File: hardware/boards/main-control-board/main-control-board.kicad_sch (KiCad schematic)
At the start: 7 parts, among them J2 Conn_OLED, J3 Conn_extension, J4 Conn_extension_2

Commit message: pre-fab improvements
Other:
- sheet ESP32 ports: added USB_DP; removed UDB_DP
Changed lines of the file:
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@@
 	(title_block
 		(title "TinyEngineer PCB")
-		(date "2026-09-12")
-		(rev "v1")
+		(date "2026-09-24")
+		(rev "v2")
 	)
 	(junction
@@
 			)
 		)
-		(pin "USB_D-" input
+		(pin "USB_D-" bidirectional
 			(at 224.79 95.25 180)
 			(effects
@@
 			)
 		)
-		(pin "USB_D+" input
+		(pin "USB_D+" bidirectional
 			(at 224.79 92.71 180)
 			(effects
@@
 			)
 		)
-		(pin "GP0" input
+		(pin "GP0" bidirectional
 			(at 139.7 87.63 180)
 			(effects
@@
 			)
 		)
-		(pin "GP2" input
+		(pin "GP2" bidirectional
 			(at 139.7 97.79 180)
 			(effects
@@
 			)
 		)
-		(pin "GP1" input
+		(pin "GP1" bidirectional
 			(at 139.7 90.17 180)
 			(effects
@@
 			)
 		)
-		(pin "UDB_DP" input
+		(pin "USB_DM" bidirectional
+			(at 186.69 95.25 0)
+			(effects
+				(font
+					(size 1.27 1.27)
+				)
+				(justify right)
+			)
+		)
+		(pin "GP5" bidirectional
+			(at 139.7 92.71 180)
+			(effects
+				(font
+					(size 1.27 1.27)
+				)
+				(justify left)
+			)
+		)
+		(pin "GP4" bidirectional
+			(at 139.7 102.87 180)
+			(effects
+				(font
+					(size 1.27 1.27)
+				)
+				(justify left)
+			)
+		)
+		(pin "GP3" bidirectional
+			(at 139.7 100.33 180)
+			(effects
+				(font
+					(size 1.27 1.27)
+				)
+				(justify left)
+			)
+		)
+		(pin "GP6" bidirectional
+			(at 186.69 87.63 0)
+			(effects
+				(font
+					(size 1.27 1.27)
+				)
+				(justify right)
+			)
+		)
+		(pin "USB_DP" bidirectional
 			(at 186.69 92.71 0)
-			(effects
-				(font
-					(size 1.27 1.27)
-				)
-				(justify right)
-			)
-		)
-		(pin "USB_DM" input
-			(at 186.69 95.25 0)
-			(effects
-				(font
-					(size 1.27 1.27)
-				)
-				(justify right)
-			)
-		)
-		(pin "GP5" input
-			(at 139.7 92.71 180)
-			(effects
-				(font
-					(size 1.27 1.27)
-				)
-				(justify left)
-			)
-		)
-		(pin "GP4" input
-			(at 139.7 102.87 180)
-			(effects
-				(font
-					(size 1.27 1.27)
-				)
-				(justify left)
-			)
-		)
-		(pin "GP3" input
-			(at 139.7 100.33 180)
-			(effects
-				(font
-					(size 1.27 1.27)
-				)
-				(justify left)
-			)
-		)
-		(pin "GP6" input
-			(at 186.69 87.63 0)
 			(effects
 				(font
@@
 			)
 		)
-		(pin "SCL" input
+		(pin "SCL" bidirectional
 			(at 99.06 90.17 0)
 			(effects
@@
 			)
 		)
-		(pin "SDA" input
+		(pin "SDA" bidirectional
 			(at 99.06 87.63 0)
 			(effects

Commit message: fix expected nets
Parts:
- added H3: MountingHole, MountingHole:MountingHole_2.2mm_M2, symbol Mechanical:MountingHole
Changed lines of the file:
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@@
+	(symbol
+		(lib_id "Mechanical:MountingHole")
+		(at 68.58 60.96 0)
+		(unit 1)
+		(body_style 1)
+		(exclude_from_sim no)
+		(in_bom no)
+		(on_board yes)
+		(in_pos_files no)
+		(dnp no)
+		(fields_autoplaced yes)
+		(property "Reference" "H3"
+			(at 71.12 59.6899 0)
+			(show_name no)
+			(do_not_autoplace no)
+			(effects
+				(font
+					(size 1.27 1.27)
+				)
+				(justify left)
+			)
+		)
+		(property "Value" "MountingHole"
+			(at 71.12 62.2299 0)
+			(show_name no)
+			(do_not_autoplace no)
+			(effects
+				(font
+					(size 1.27 1.27)
+				)
+				(justify left)
+			)
+		)
+		(property "Footprint" "MountingHole:MountingHole_2.2mm_M2"
+			(at 68.58 60.96 0)
+			(hide yes)
+			(show_name no)
+			(do_not_autoplace no)
+			(effects
+				(font
+					(size 1.27 1.27)
+				)
+			)
+		)
+		(property "Datasheet" ""
+			(at 68.58 60.96 0)
+			(hide yes)
+			(show_name no)
+			(do_not_autoplace no)
+			(effects
+				(font
+					(size 1.27 1.27)
+				)
+			)
+		)
+		(property "Description" "Mounting Hole without connection"
+			(at 68.58 60.96 0)
+			(hide yes)
+			(show_name no)
+			(do_not_autoplace no)
+			(effects
+				(font
+					(size 1.27 1.27)
+				)
+			)
+		)
+		(instances
+			(project "main-control-board"
+				(path "/82a78d11-58ff-455c-a94e-f7463ce9fc2e"
+					(reference "H3")
+					(unit 1)
+				)
+			)
+		)
+	)
 	(symbol
 		(lib_id "Mechanical:MountingHole")

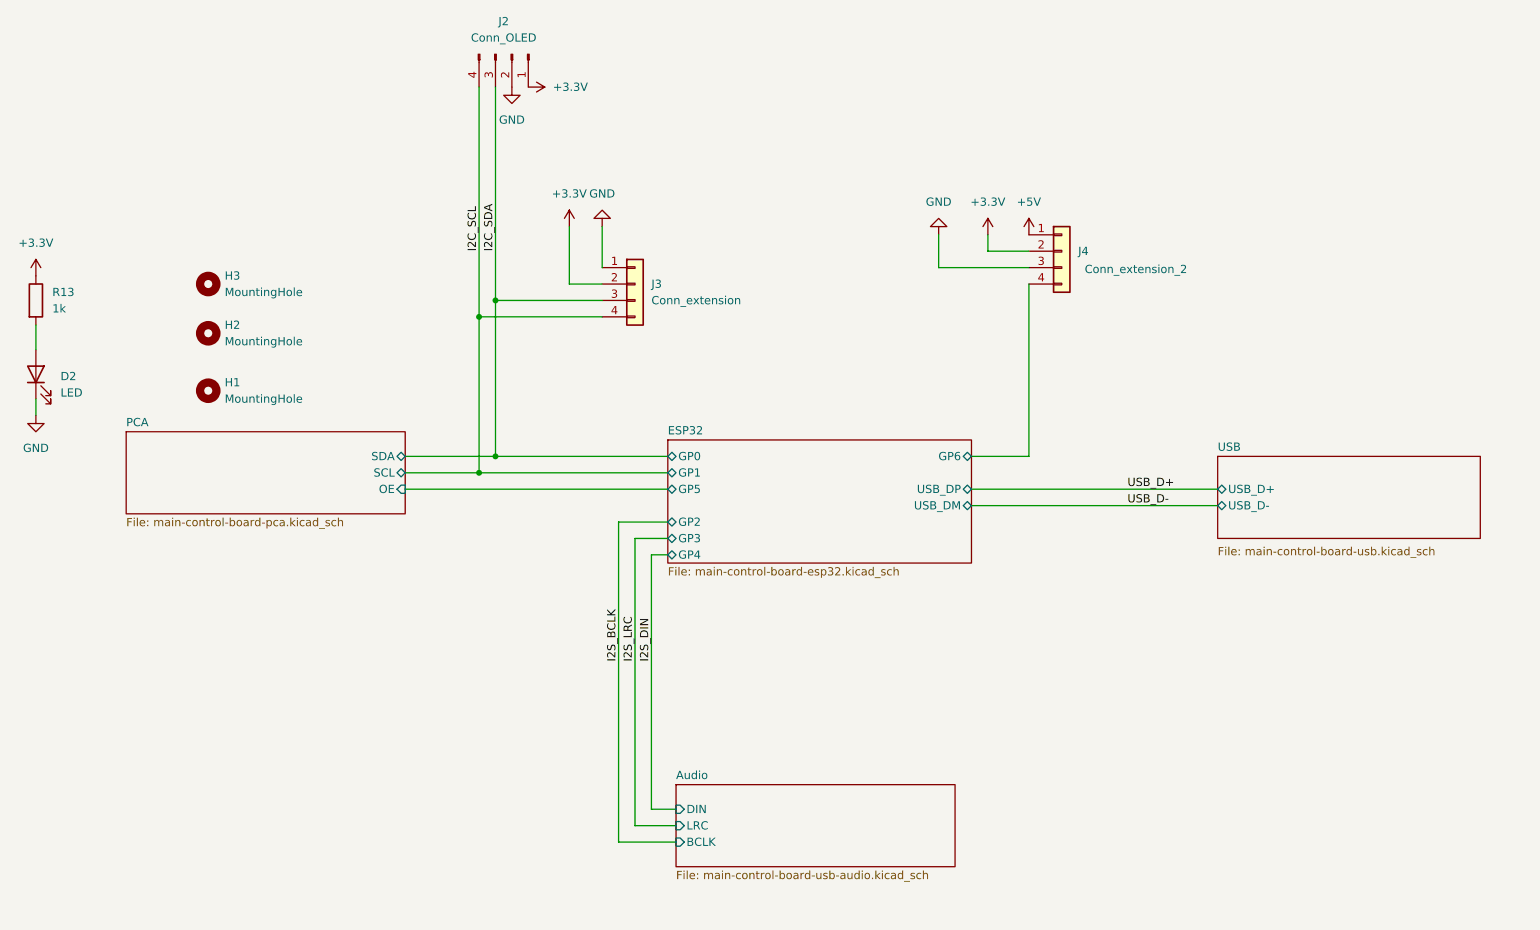
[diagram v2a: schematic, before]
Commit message: add efuse before 5V servo rail
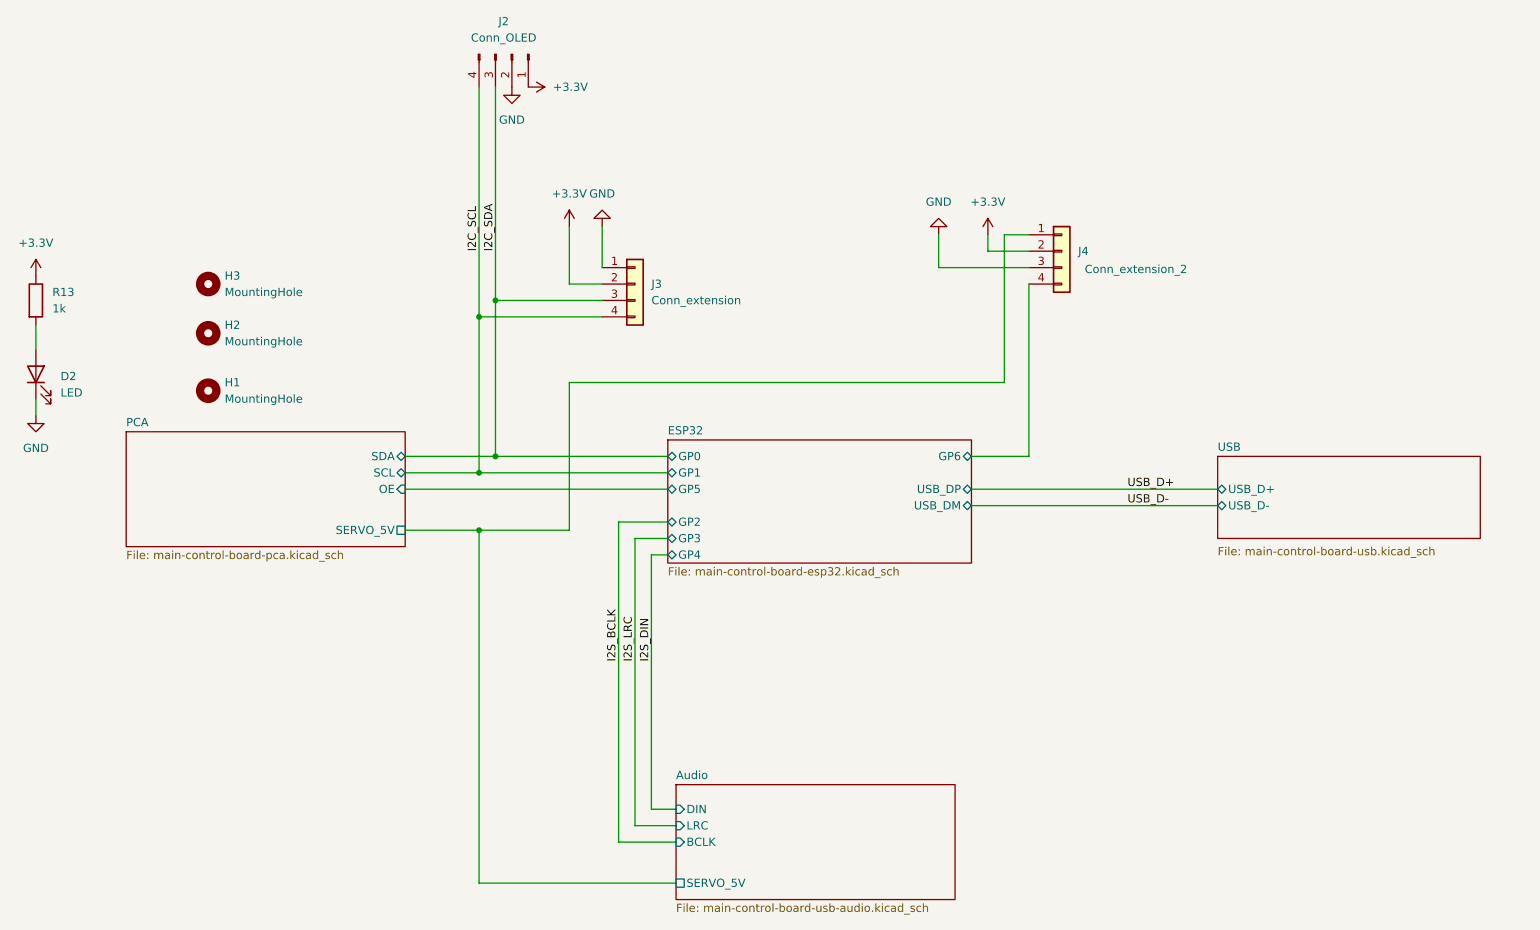
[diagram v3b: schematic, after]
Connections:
- net +5V renamed Audio/SERVO_5V
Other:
- sheet Audio ports: added SERVO_5V; removed none
- sheet PCA ports: added SERVO_5V; removed none
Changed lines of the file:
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@@
+	)
+	(junction
+		(at 110.49 99.06)
+		(diameter 0)
+		(color 0 0 0 0)
 	)
 	(junction
@@
 	(wire
 		(pts
+			(xy 191.77 76.2) (xy 124.46 76.2)
+		)
+		(stroke
+			(width 0)
+			(type default)
+		)
+	)
+	(wire
+		(pts
 			(xy 99.06 92.71) (xy 139.7 92.71)
 		)
@@
 	(wire
 		(pts
+			(xy 99.06 99.06) (xy 110.49 99.06)
+		)
+		(stroke
+			(width 0)
+			(type default)
+		)
+	)
+	(wire
+		(pts
+			(xy 124.46 76.2) (xy 124.46 99.06)
+		)
+		(stroke
+			(width 0)
+			(type default)
+		)
+	)
+	(wire
+		(pts
 			(xy 132.08 147.32) (xy 140.97 147.32)
 		)
@@
 	(wire
 		(pts
+			(xy 140.97 153.67) (xy 110.49 153.67)
+		)
+		(stroke
+			(width 0)
+			(type default)
+		)
+	)
+	(wire
+		(pts
 			(xy 195.58 87.63) (xy 186.69 87.63)
 		)
@@
 	(wire
 		(pts
+			(xy 110.49 153.67) (xy 110.49 99.06)
+		)
+		(stroke
+			(width 0)
+			(type default)
+		)
+	)
+	(wire
+		(pts
 			(xy 181.61 58.42) (xy 195.58 58.42)
 		)
@@
 		(pts
 			(xy 186.69 95.25) (xy 224.79 95.25)
+		)
+		(stroke
+			(width 0)
+			(type default)
+		)
+	)
+	(wire
+		(pts
+			(xy 195.58 53.34) (xy 191.77 53.34)
+		)
+		(stroke
+			(width 0)
+			(type default)
+		)
+	)
+	(wire
+		(pts
+			(xy 124.46 99.06) (xy 110.49 99.06)
+		)
+		(stroke
+			(width 0)
+			(type default)
+		)
+	)
+	(wire
+		(pts
+			(xy 191.77 53.34) (xy 191.77 76.2)
 		)
 		(stroke
@@
 	)
 	(symbol
-		(lib_id "power:+5V")
-		(at 195.58 53.34 0)
-		(unit 1)
-		(body_style 1)
-		(exclude_from_sim no)
-		(in_bom yes)
-		(on_board yes)
-		(in_pos_files yes)
-		(dnp no)
-		(fields_autoplaced yes)
-		(property "Reference" "#PWR011"
-			(at 195.58 57.15 0)
-			(hide yes)
-			(show_name no)
-			(do_not_autoplace no)
-			(effects
-				(font
-					(size 1.27 1.27)
-				)
-			)
-		)
-		(property "Value" "+5V"
-			(at 195.58 48.26 0)
-			(show_name no)
-			(do_not_autoplace no)
-			(effects
-				(font
-					(size 1.27 1.27)
-				)
-			)
-		)
-		(property "Footprint" ""
-			(at 195.58 53.34 0)
-			(hide yes)
-			(show_name no)
-			(do_not_autoplace no)
-			(effects
-				(font
-					(size 1.27 1.27)
-				)
-			)
-		)
-		(property "Datasheet" ""
-			(at 195.58 53.34 0)
-			(hide yes)
-			(show_name no)
-			(do_not_autoplace no)
-			(effects
-				(font
-					(size 1.27 1.27)
-				)
-			)
-		)
-		(property "Description" "Power symbol creates a global label with name \"+5V\""
-			(at 195.58 53.34 0)
-			(hide yes)
-			(show_name no)
-			(do_not_autoplace no)
-			(effects
-				(font
-					(size 1.27 1.27)
-				)
-			)
-		)
-		(pin "1"
-		)
-		(instances
-			(project "main-control-board"
-				(path "/82a78d11-58ff-455c-a94e-f7463ce9fc2e"
-					(reference "#PWR011")
-					(unit 1)
-				)
-			)
-		)
-	)
-	(symbol
 		(lib_id "Mechanical:MountingHole")
 		(at 68.58 60.96 0)
@@
 	(sheet
 		(at 55.88 83.82)
-		(size 43.18 12.7)
+		(size 43.18 17.78)
 		(exclude_from_sim no)
 		(in_bom yes)
@@
 		)
 		(property "Sheetfile" "main-control-board-pca.kicad_sch"
-			(at 55.88 97.1046 0)
+			(at 55.88 102.1846 0)
 			(show_name no)
 			(do_not_autoplace no)
@@
 		(pin "SDA" bidirectional
 			(at 99.06 87.63 0)
+			(effects
+				(font
+					(size 1.27 1.27)
+				)
+				(justify right)
+			)
+		)
+		(pin "SERVO_5V" passive
+			(at 99.06 99.06 0)
 			(effects
 				(font
@@
 	(sheet
 		(at 140.97 138.43)
-		(size 43.18 12.7)
+		(size 43.18 17.78)
 		(exclude_from_sim no)
 		(in_bom yes)
@@
 		)
 		(property "Sheetfile" "main-control-board-usb-audio.kicad_sch"
-			(at 140.97 151.7146 0)
+			(at 140.97 156.7946 0)
 			(show_name no)
 			(do_not_autoplace no)
@@
 			(effects
 				(font
+					(size 1.27 1.27)
+				)
+				(justify left)
+			)
+		)
+		(pin "SERVO_5V" passive
+			(at 140.97 153.67 180)
+			(effects
+				(font

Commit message: feat(pcb): update component properties and add missing attributes
- Renamed connection values for ESP32 components to standardize naming.
- Added properties for KiLib_Generator, MPN, and Manufacturer for various components across multiple schematic files.
- Enhanced documentation for component attributes to improve clarity and accessibility in the design process.
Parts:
- D2: MPN (none) -> KT-0603R; Manufacturer (none) -> Hubei KENTO Elec
- J2: MPN (none) -> PZ254V-11-04P; Manufacturer (none) -> XFCN
- J3: MPN (none) -> SM04B-SRSS-TB(LF)(SN); Manufacturer (none) -> JST
- R13: MPN (none) -> 0603WAF1001T5E; Manufacturer (none) -> UNI-ROYAL(Uniroyal Elec)
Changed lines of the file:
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@@
+			)
+		)
+		(property "KiLib_Generator" ""
+			(at 134.62 60.96 0)
+			(hide yes)
+			(show_name no)
+			(do_not_autoplace no)
+			(effects
+				(font
+					(size 1.27 1.27)
+				)
+			)
+		)
+		(property "MPN" "SM04B-SRSS-TB(LF)(SN)"
+			(at 134.62 60.96 0)
+			(hide yes)
+			(show_name no)
+			(do_not_autoplace no)
+			(effects
+				(font
+					(size 1.27 1.27)
+				)
+			)
+		)
+		(property "Manufacturer" "JST"
+			(at 134.62 60.96 0)
+			(hide yes)
+			(show_name no)
+			(do_not_autoplace no)
+			(effects
+				(font
+					(size 1.27 1.27)
+				)
 			)
 		)
@@
 			)
 		)
+		(property "KiLib_Generator" ""
+			(at 115.57 25.4 90)
+			(hide yes)
+			(show_name no)
+			(do_not_autoplace no)
+			(effects
+				(font
+					(size 1.27 1.27)
+				)
+			)
+		)
+		(property "MPN" "PZ254V-11-04P"
+			(at 115.57 25.4 90)
+			(hide yes)
+			(show_name no)
+			(do_not_autoplace no)
+			(effects
+				(font
+					(size 1.27 1.27)
+				)
+			)
+		)
+		(property "Manufacturer" "XFCN"
+			(at 115.57 25.4 90)
+			(hide yes)
+			(show_name no)
+			(do_not_autoplace no)
+			(effects
+				(font
+					(size 1.27 1.27)
+				)
+			)
+		)
 		(pin "4"
 		)
@@
 			)
 		)
+		(property "KiLib_Generator" ""
+			(at 41.91 63.5 0)
+			(hide yes)
+			(show_name no)
+			(do_not_autoplace no)
+			(effects
+				(font
+					(size 1.27 1.27)
+				)
+			)
+		)
+		(property "MPN" "0603WAF1001T5E"
+			(at 41.91 63.5 0)
+			(hide yes)
+			(show_name no)
+			(do_not_autoplace no)
+			(effects
+				(font
+					(size 1.27 1.27)
+				)
+			)
+		)
+		(property "Manufacturer" "UNI-ROYAL(Uniroyal Elec)"
+			(at 41.91 63.5 0)
+			(hide yes)
+			(show_name no)
+			(do_not_autoplace no)
+			(effects
+				(font
+					(size 1.27 1.27)
+				)
+			)
+		)
 		(pin "1"
 		)
@@
 			)
 		)
+		(property "KiLib_Generator" ""
+			(at 68.58 60.96 0)
+			(hide yes)
+			(show_name no)
+			(do_not_autoplace no)
+			(effects
+				(font
+					(size 1.27 1.27)
+				)
+			)
+		)
 		(instances
 			(project "main-control-board"
@@
 			)
 		)
+		(property "KiLib_Generator" ""
+			(at 68.58 77.47 0)
+			(hide yes)
+			(show_name no)
+			(do_not_autoplace no)
+			(effects
+				(font
+					(size 1.27 1.27)
+				)
+			)
+		)
 		(instances
 			(project "main-control-board"
@@
 			)
 		)
+		(property "KiLib_Generator" ""
+			(at 41.91 74.93 90)
+			(hide yes)
+			(show_name no)
+			(do_not_autoplace no)
+			(effects
+				(font
+					(size 1.27 1.27)
+				)
+			)
+		)
+		(property "MPN" "KT-0603R"
+			(at 41.91 74.93 90)
+			(hide yes)
+			(show_name no)
+			(do_not_autoplace no)
+			(effects
+				(font
+					(size 1.27 1.27)
+				)
+			)
+		)
+		(property "Manufacturer" "Hubei KENTO Elec"
+			(at 41.91 74.93 90)
+			(hide yes)
+			(show_name no)
+			(do_not_autoplace no)
+			(effects
+				(font
+					(size 1.27 1.27)
+				)
+			)
+		)
 		(pin "1"
 		)
@@
 		)
 		(property "Description" "Generic connector, single row, 01x04, script generated (kicad-library-utils/schlib/autogen/connector/)"
+			(at 200.66 55.88 0)
+			(hide yes)
+			(show_name no)
+			(do_not_autoplace no)
+			(effects
+				(font
+					(size 1.27 1.27)
+				)
+			)
+		)
+		(property "KiLib_Generator" ""
 			(at 200.66 55.88 0)
 			(hide yes)
@@
 			(at 68.58 68.58 0)
 			(hide yes)
+			(show_name no)
+			(do_not_autoplace no)
+			(effects
+				(font
+					(size 1.27 1.27)
+				)
+			)
+		)
+		(property "KiLib_Generator" ""
+			(at 68.58 68.58 0)
+			(hide yes)
